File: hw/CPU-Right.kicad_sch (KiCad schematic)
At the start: 24 parts, among them J1100 Conn_01x08, J1101 Conn_01x02, J1102 Conn_01x02, J1103 Conn_01x02, J1104 Conn_01x02, U1100 STM32F401XX-LQFP100, Y1100 MCSJK-7I-8.00-18-30-60-B-30

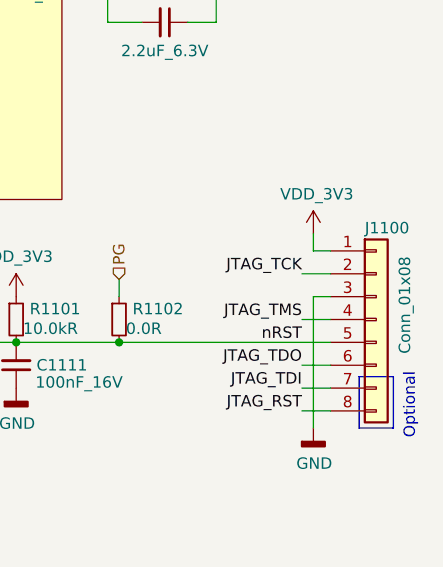
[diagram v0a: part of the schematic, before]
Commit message: Replace JTAG connectors with angled ones one back side.
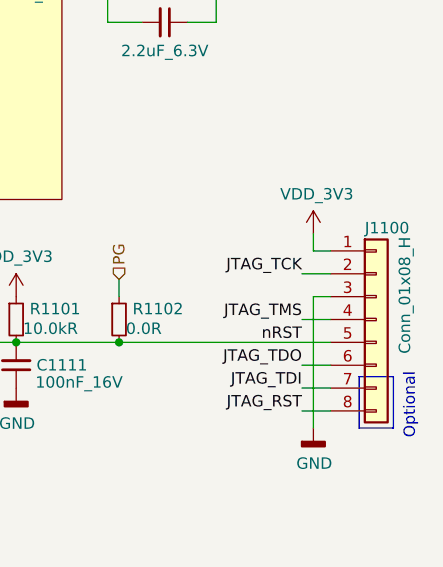
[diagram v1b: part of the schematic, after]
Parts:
- J1100: value Conn_01x08 -> Conn_01x08_H; footprint Keyboard:Pin_Header_Straight_1x08_Pitch2.54mm -> Keyboard:Pin_Header_Horizontal_1x08_Pitch2.54mm; symbol Keyboard:Conn_01x08 -> Keyboard:Conn_01x08_H; farnell# 1593416 -> 1593431
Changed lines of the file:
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@@
     )
   )
-  (symbol (lib_id "Keyboard:Conn_01x08") (at 276.225 140.335 0) (unit 1)
+  (symbol (lib_id "Keyboard:Conn_01x08_H") (at 276.225 140.335 0) (unit 1)
     (in_bom yes) (on_board yes) (dnp no)
     (property "Reference" "J1100" (at 274.955 130.175 0)
       (effects (font (size 1.27 1.27)) (justify left))
     )
-    (property "Value" "Conn_01x08" (at 279.4 144.145 90)
+    (property "Value" "Conn_01x08_H" (at 279.4 144.145 90)
       (effects (font (size 1.27 1.27)) (justify left))
     )
-    (property "Footprint" "Keyboard:Pin_Header_Straight_1x08_Pitch2.54mm" (at 273.685 132.715 0)
+    (property "Footprint" "Keyboard:Pin_Header_Horizontal_1x08_Pitch2.54mm" (at 273.685 132.715 0)
       (effects (font (size 1.27 1.27)) hide)
     )
-    (property "Datasheet" "Multicomp  2211S-08G" (at 276.225 130.175 0)
+    (property "Datasheet" "Multicomp  34753" (at 276.225 130.175 0)
       (effects (font (size 1.27 1.27)) hide)
     )
-    (property "farnell#" "1593416" (at 276.225 127.635 0)
+    (property "farnell#" "1593431" (at 276.225 127.635 0)
       (effects (font (size 1.524 1.524)) hide)
     )
